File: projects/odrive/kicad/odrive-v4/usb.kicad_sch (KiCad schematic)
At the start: 14 parts, among them J6 USB4105-GF-A, U33 USBLC6-2SC6

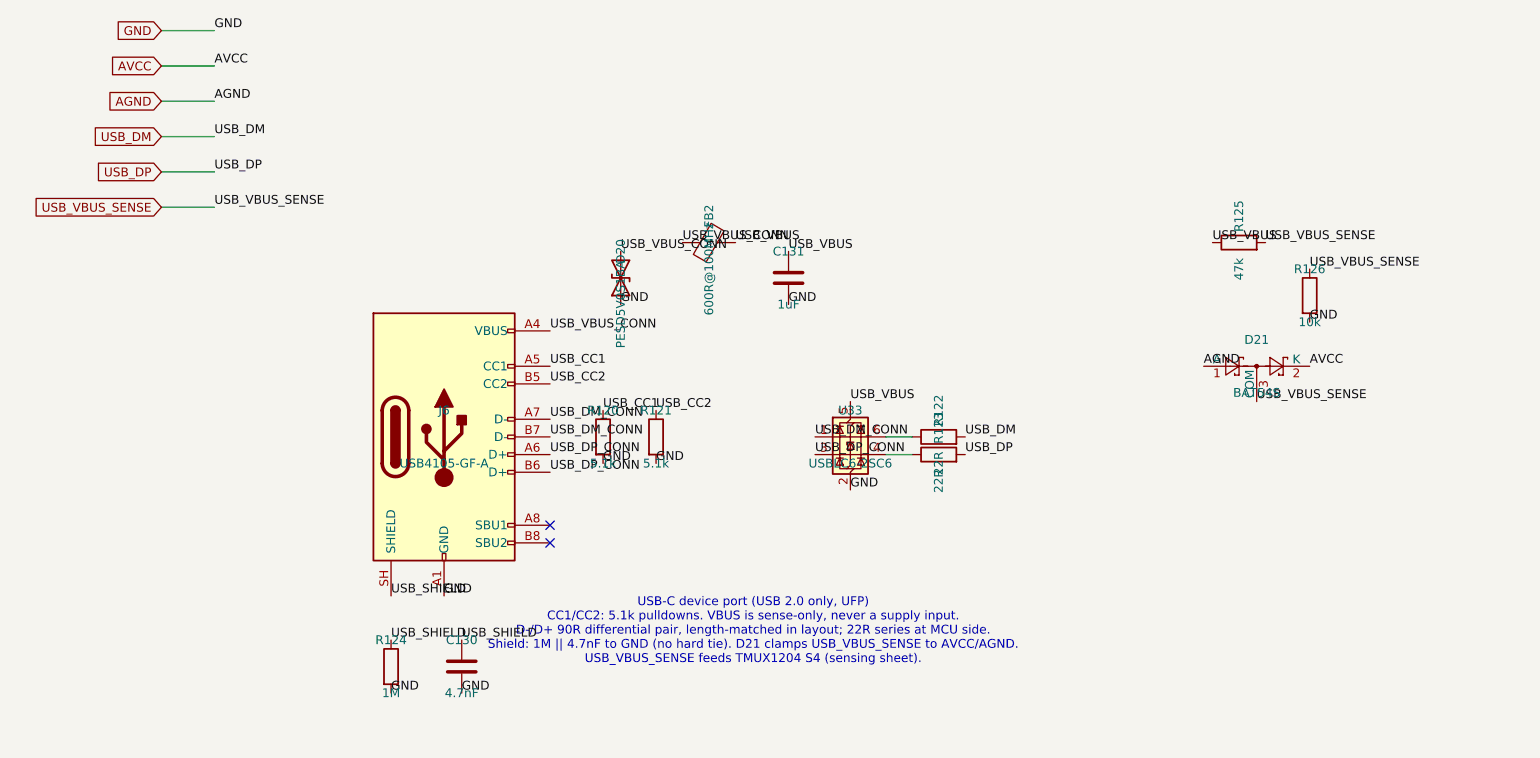
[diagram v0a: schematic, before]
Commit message: Make the v4 schematic sheets readable, netlist-invariant
The verified v4 schematic was electrically perfect and visually unreadable:
connectivity lived in labels stuck on pins, text overlapped, and parts sat
on the title block. Reworked all ten block sheets through Konnect: real
wires for local connections, labels kept for power rails and inter-sheet
nets, parts grouped by function, junction dots where wires join.

The invariant was enforced, not assumed: the exported netlist is diffed
against a reference frozen before the rework - 378 components and 283 nets,
identical membership pin by pin - and ERC holds at 0 errors. The lesson
that forced the rework is now a standing gate: numeric oracles (ERC,
netlist diff, overlap counts) all passed on the unreadable version, so
every sheet is also rendered to PNG and looked at before being declared
done.

An interrupted fix round left one known cosmetic issue, documented in
docs/LOG.md: the encoders-gpio GPIO group's reference/value text fields
float ~134mm right of their symbols, over the title block. konnect 0.2.2
has no tool that repositions property fields, so it waits for 0.11.0.
Also adds the fab footprints the sheets reference (MEGA fuse, Phoenix
terminal blocks, CMC) and restores the board file to the blank template -
the aborted layout skeleton was not worth keeping.
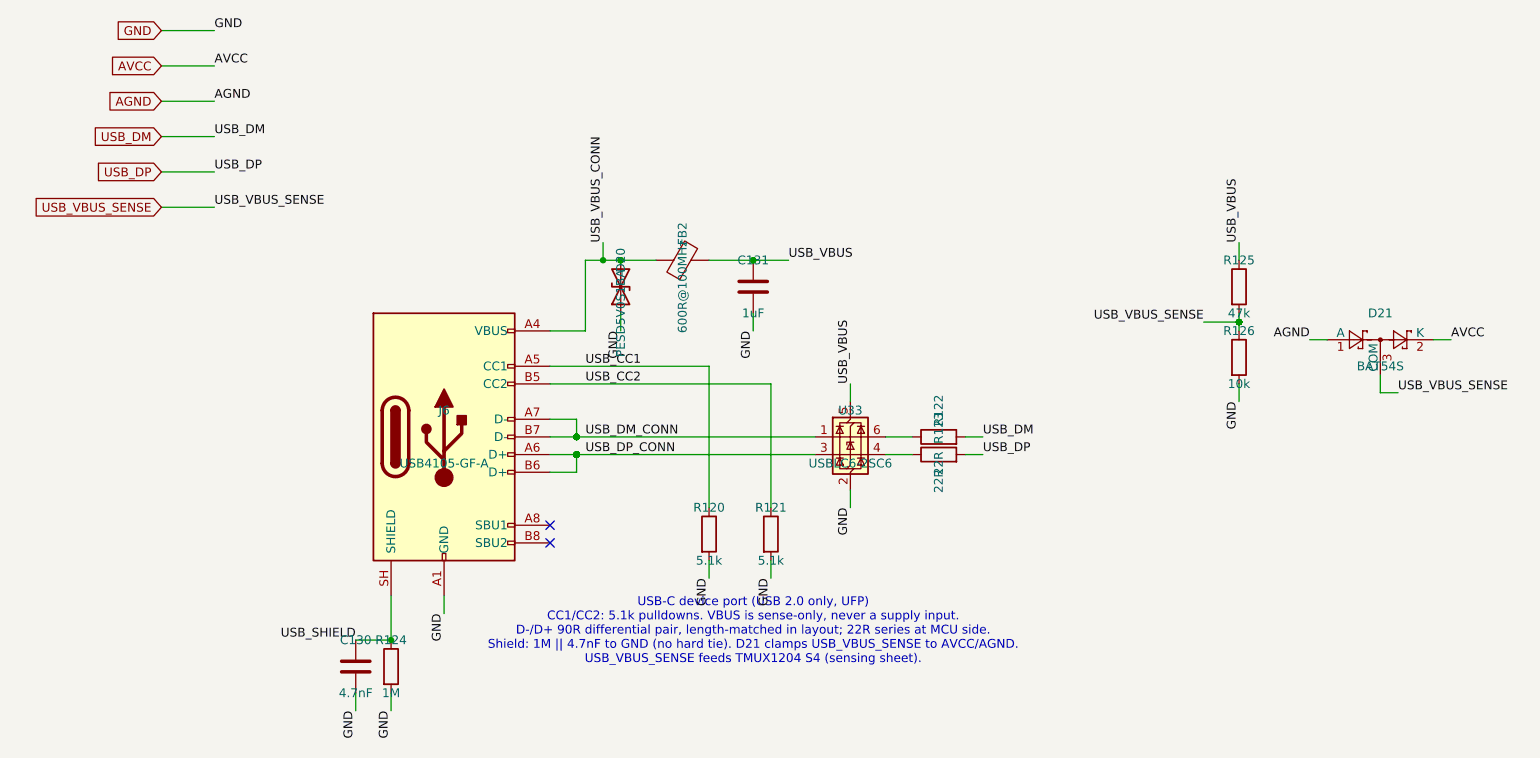
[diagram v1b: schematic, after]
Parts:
- C130, C131: footprint (none) -> Capacitor_SMD:C_0603_1608Metric
- D20: footprint (none) -> Diode_SMD:D_SOD-323
- D21: footprint (none) -> Package_TO_SOT_SMD:SOT-23
- FB2: footprint (none) -> Inductor_SMD:L_0805_2012Metric
- J6: footprint (none) -> Connector_USB:USB_C_Receptacle_GCT_USB4105-xx-A_16P_TopMnt_Horizontal
- R120, R121, R122, R123, R124, R125, R126: footprint (none) -> Resistor_SMD:R_0603_1608Metric
- U33: footprint (none) -> Package_TO_SOT_SMD:SOT-23-6
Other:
- moved on the sheet: C130, C131, D20, D21, FB2, R120, R121, R125, R126
